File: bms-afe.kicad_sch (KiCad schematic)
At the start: 0 parts

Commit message: mostly done afe ic
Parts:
- added J2: CONN HEADER VERT 7POS 2.5MM, footprints:JST_B7B-XH-A_LF__SN_, symbol symbols:B7B-XH-A_LF__SN_
- added R39: R_Small_US, symbol Device:R_Small_US
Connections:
- new net AFEIC/U12P: J2.7, R39.1
- new net BAT_GND: J2.1
- new net CellBalance/Battery_Bottom: J2.6
- new net CellBalance1/Battery_Bottom: J2.5
- new net CellBalance2/Battery_Bottom: J2.4
- new net CellBalance3/Battery_Bottom: J2.3
- new net CellBalance4/Battery_Bottom: J2.2
- new net VBLK: R39.2
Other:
- removed sheet Balancing
- added sheet AFEIC (AFEIC.kicad_sch)
- added sheet CellBalance (CellBalance.kicad_sch)
- added sheet CellBalance1 (CellBalance.kicad_sch)
- added sheet CellBalance2 (CellBalance.kicad_sch)
- added sheet CellBalance3 (CellBalance.kicad_sch)
- added sheet CellBalance4 (CellBalance.kicad_sch)
- added sheet CellBalance5 (CellBalance.kicad_sch)

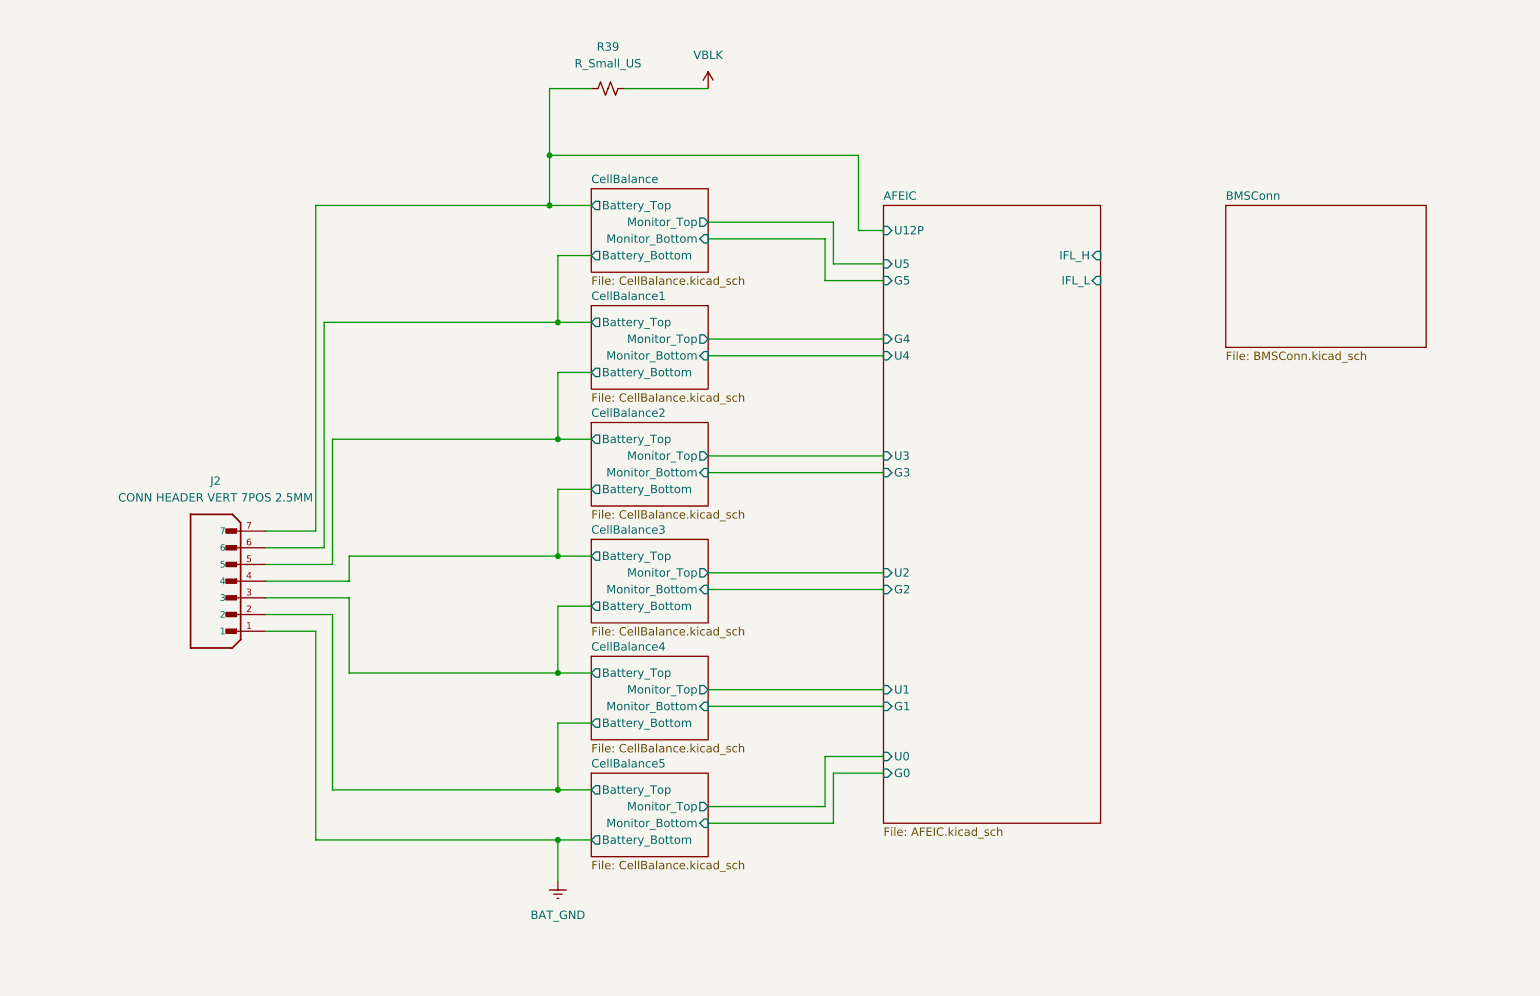
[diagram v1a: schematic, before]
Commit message: schematic done except for pulse transformer
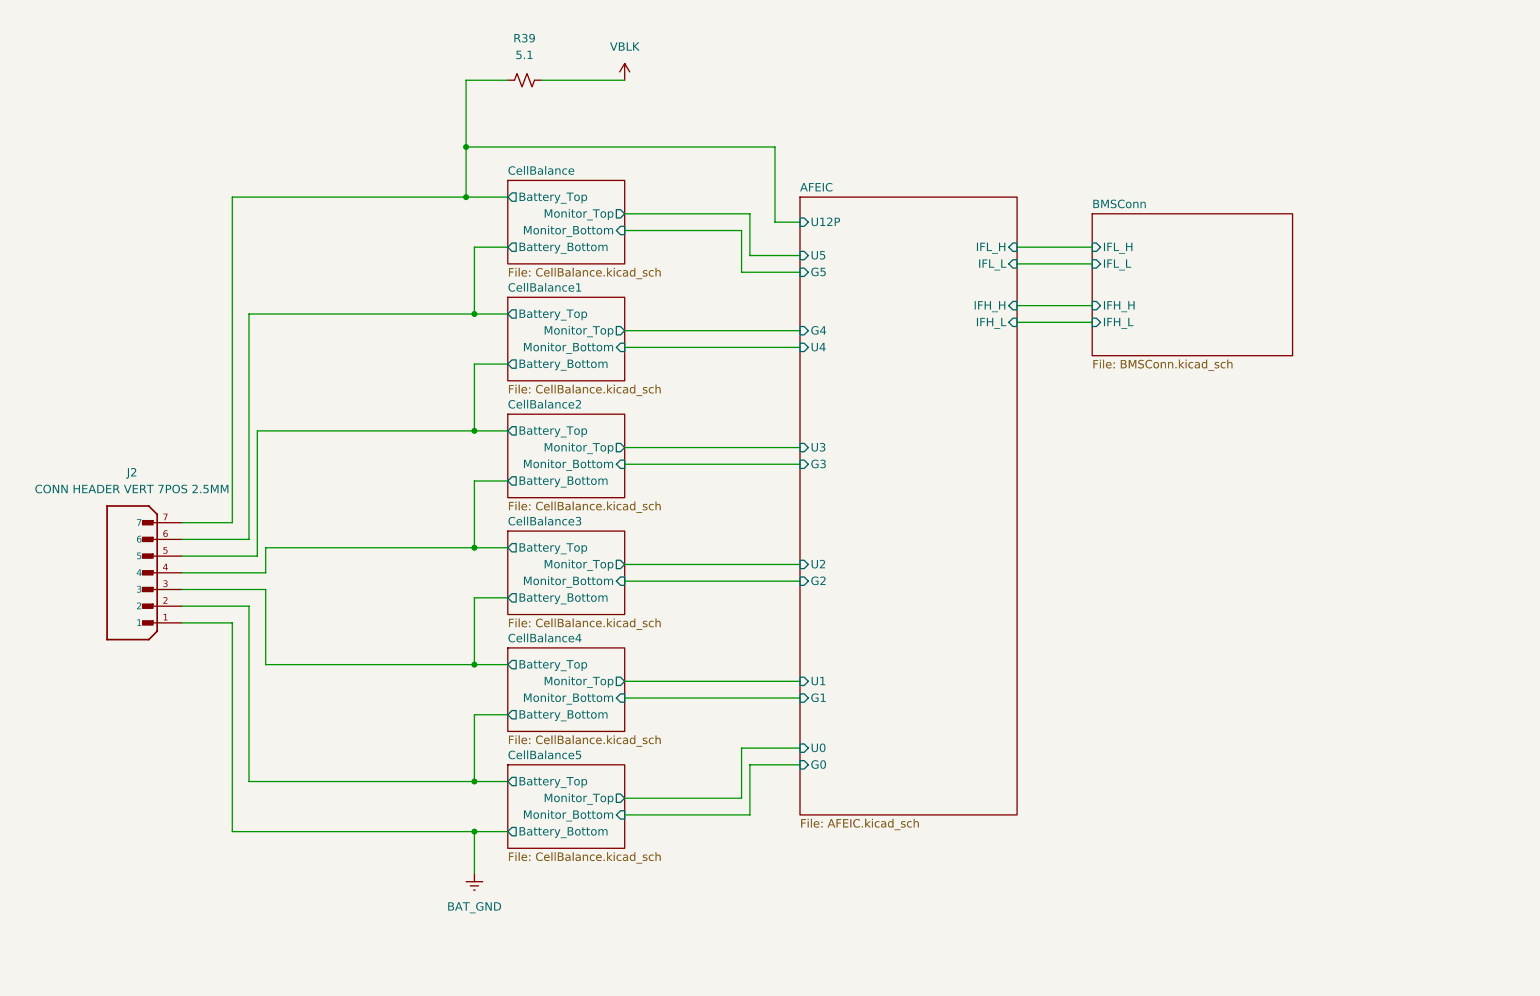
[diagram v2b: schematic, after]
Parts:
- R39: value R_Small_US -> 5.1
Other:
- sheet AFEIC ports: added IFH_H, IFH_L; removed none
- sheet BMSConn ports: added IFH_H, IFH_L, IFL_H, IFL_L; removed none
- moved on the sheet: J2, R39

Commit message: fixed balancing module and added pulse transformer
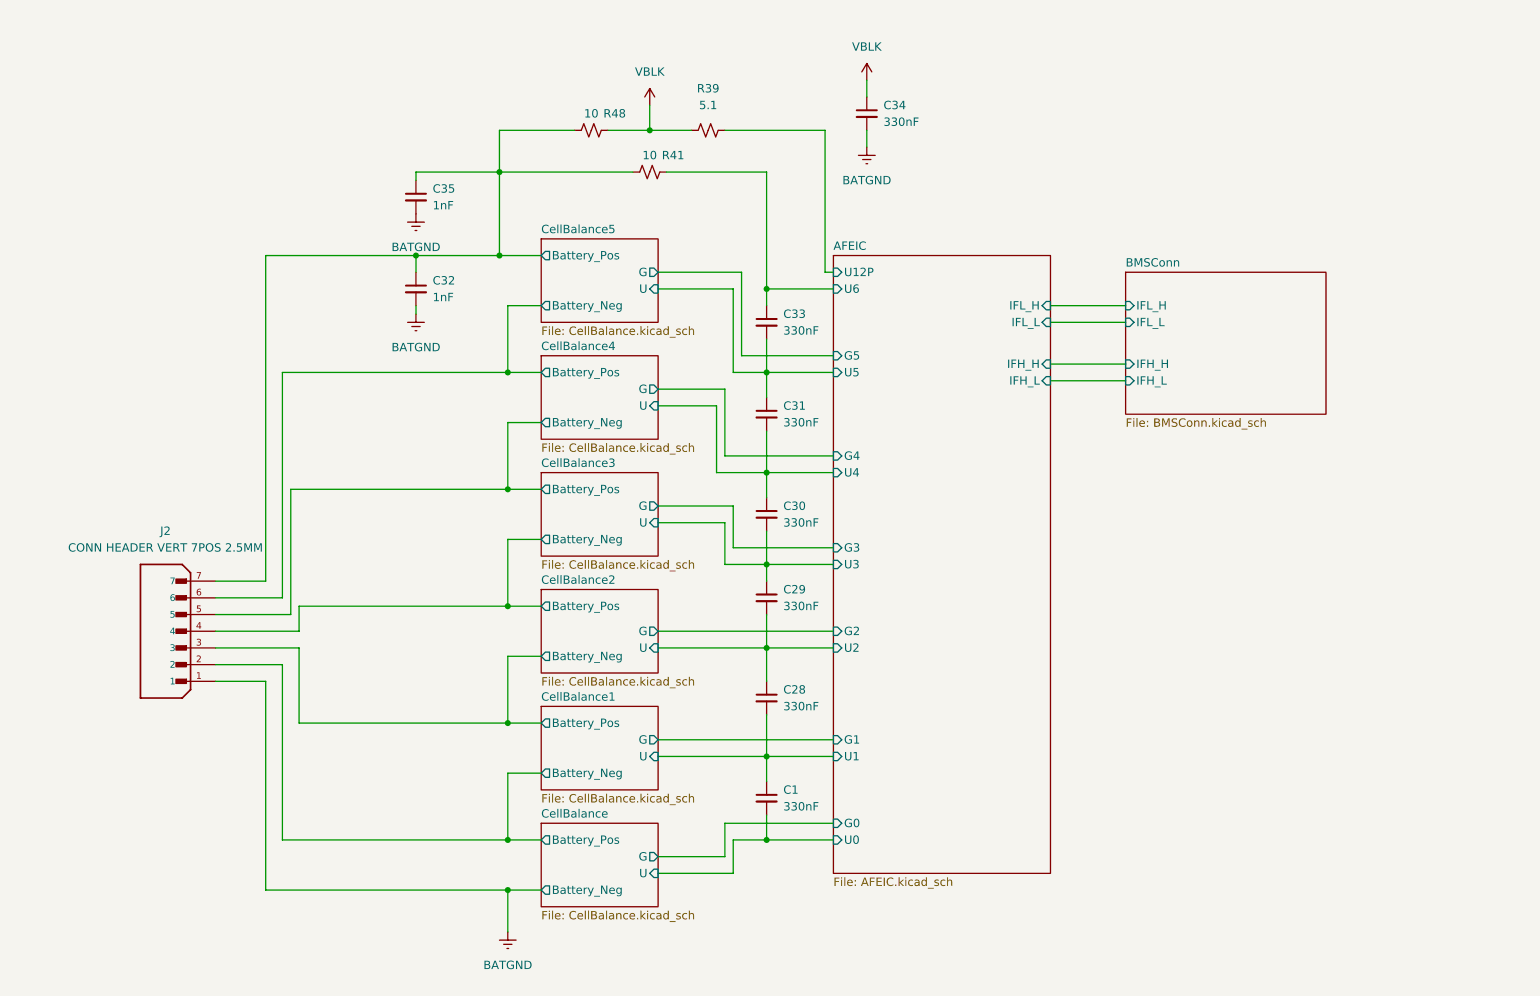
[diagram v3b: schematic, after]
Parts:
- added C1, C28, C29, C30, C31, C33, C34: 330nF, symbol Device:C_Small
- added C32, C35: 1nF, symbol Device:C_Small
- added R41, R48: 10, symbol Device:R_Small_US
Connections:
- net AFEIC/U0: now also C1.2
- net AFEIC/U1: now also C1.1, C28.2
- net AFEIC/U12P: now also R39.2; no longer J2.7, R39.1
- net AFEIC/U2: now also C28.1, C29.2
- net AFEIC/U3: now also C29.1, C30.2
- net AFEIC/U4: now also C30.1, C31.2
- net AFEIC/U5: now also C31.1, C33.2
- net VBLK: now also R39.1, C34.1, R48.2; no longer R39.2
- net BAT_GND renamed BATGND
- net BATGND: now also C32.2, C34.2, C35.2
- net CellBalance/Battery_Bottom renamed CellBalance4/Battery_Pos
- net CellBalance1/Battery_Bottom renamed CellBalance3/Battery_Pos
- net CellBalance2/Battery_Bottom renamed CellBalance2/Battery_Pos
- net CellBalance3/Battery_Bottom renamed CellBalance1/Battery_Pos
- net CellBalance4/Battery_Bottom renamed CellBalance/Battery_Pos
- new net AFEIC/U6: C33.1, R41.2
- new net CellBalance5/Battery_Pos: C32.1, C35.1, J2.7, R41.1, R48.1
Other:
- sheet AFEIC ports: added U6; removed none
- sheet CellBalance ports: added Battery_Neg, Battery_Pos, G, U; removed Battery_Bottom, Battery_Top, Monitor_Bottom, Monitor_Top
- sheet CellBalance1 ports: added Battery_Neg, Battery_Pos, G, U; removed Battery_Bottom, Battery_Top, Monitor_Bottom, Monitor_Top
- sheet CellBalance2 ports: added Battery_Neg, Battery_Pos, G, U; removed Battery_Bottom, Battery_Top, Monitor_Bottom, Monitor_Top
- sheet CellBalance3 ports: added Battery_Neg, Battery_Pos, G, U; removed Battery_Bottom, Battery_Top, Monitor_Bottom, Monitor_Top
- sheet CellBalance4 ports: added Battery_Neg, Battery_Pos, G, U; removed Battery_Bottom, Battery_Top, Monitor_Bottom, Monitor_Top
- sheet CellBalance5 ports: added Battery_Neg, Battery_Pos, G, U; removed Battery_Bottom, Battery_Top, Monitor_Bottom, Monitor_Top
- moved on the sheet: J2

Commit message: finished schematic
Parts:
- renumbered C35 to C1, C32 to C2, C33 to C3, C31 to C4, C30 to C5, C29 to C6, C28 to C7, C1 to C8, C34 to C9, J2 to J1, R48 to R1, R41 to R2, R39 to R3
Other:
- moved on the sheet: R2
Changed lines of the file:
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@@
 	(wire
 		(pts
-			(xy 115.57 41.91) (xy 135.89 41.91)
+			(xy 115.57 41.91) (xy 127 41.91)
 		)
 		(stroke
@@
 	(wire
 		(pts
-			(xy 140.97 41.91) (xy 156.21 41.91)
+			(xy 132.08 41.91) (xy 156.21 41.91)
 		)
 		(stroke
@@
 		(dnp no)
 		(fields_autoplaced yes)
-		(property "Reference" "#PWR030"
+		(property "Reference" "#PWR05"
 			(at 171.45 31.75 0)
 			(hide yes)
@@
 			(project "bms-afe"
 				(path "/226a23e7-09bb-40bc-b53a-ec42a6b7cc90"
-					(reference "#PWR030")
+					(reference "#PWR05")
 					(unit 1)
 				)
@@
 		(dnp no)
 		(fields_autoplaced yes)
-		(property "Reference" "C28"
+		(property "Reference" "C7"
 			(at 158.75 120.6562 0)
 			(show_name no)
@@
 			(project "bms-afe"
 				(path "/226a23e7-09bb-40bc-b53a-ec42a6b7cc90"
-					(reference "C28")
+					(reference "C7")
 					(unit 1)
 				)
@@
 		(dnp no)
 		(fields_autoplaced yes)
-		(property "Reference" "C1"
+		(property "Reference" "C8"
 			(at 158.75 135.8962 0)
 			(show_name no)
@@
 			(project "bms-afe"
 				(path "/226a23e7-09bb-40bc-b53a-ec42a6b7cc90"
-					(reference "C1")
+					(reference "C8")
 					(unit 1)
 				)
@@
 		(dnp no)
 		(fields_autoplaced yes)
-		(property "Reference" "#PWR027"
+		(property "Reference" "#PWR02"
 			(at 102.87 69.85 0)
 			(hide yes)
@@
 			(project "bms-afe"
 				(path "/226a23e7-09bb-40bc-b53a-ec42a6b7cc90"
-					(reference "#PWR027")
+					(reference "#PWR02")
 					(unit 1)
 				)
@@
 		(dnp no)
 		(fields_autoplaced yes)
-		(property "Reference" "C35"
+		(property "Reference" "C1"
 			(at 105.41 44.4562 0)
 			(show_name no)
@@
 			(project "bms-afe"
 				(path "/226a23e7-09bb-40bc-b53a-ec42a6b7cc90"
-					(reference "C35")
+					(reference "C1")
 					(unit 1)
 				)
@@
 	(symbol
 		(lib_id "Device:R_Small_US")
-		(at 138.43 41.91 90)
-		(unit 1)
-		(body_style 1)
-		(exclude_from_sim no)
-		(in_bom yes)
-		(on_board yes)
-		(in_pos_files yes)
-		(dnp no)
-		(property "Reference" "R41"
-			(at 141.986 39.37 90)
+		(at 129.54 41.91 90)
+		(unit 1)
+		(body_style 1)
+		(exclude_from_sim no)
+		(in_bom yes)
+		(on_board yes)
+		(in_pos_files yes)
+		(dnp no)
+		(property "Reference" "R2"
+			(at 133.096 39.37 90)
 			(show_name no)
 			(do_not_autoplace no)
@@
 		)
 		(property "Value" "10"
-			(at 138.43 39.37 90)
+			(at 129.54 39.37 90)
 			(show_name no)
 			(do_not_autoplace no)
@@
 		)
 		(property "Footprint" ""
-			(at 138.43 41.91 0)
+			(at 129.54 41.91 0)
 			(hide yes)
 			(show_name no)
@@
 		)
 		(property "Datasheet" ""
-			(at 138.43 41.91 0)
+			(at 129.54 41.91 0)
 			(hide yes)
 			(show_name no)
@@
 		)
 		(property "Description" "Resistor, small US symbol"
-			(at 138.43 41.91 0)
+			(at 129.54 41.91 0)
 			(hide yes)
 			(show_name no)
@@
 			(project "bms-afe"
 				(path "/226a23e7-09bb-40bc-b53a-ec42a6b7cc90"
-					(reference "R41")
+					(reference "R2")
 					(unit 1)
 				)
@@
 		(dnp no)
 		(fields_autoplaced yes)
-		(property "Reference" "C33"
+		(property "Reference" "C3"
 			(at 158.75 63.5062 0)
 			(show_name no)
@@
 			(project "bms-afe"
 				(path "/226a23e7-09bb-40bc-b53a-ec42a6b7cc90"
-					(reference "C33")
+					(reference "C3")
 					(unit 1)
 				)
@@
 		(dnp no)
 		(fields_autoplaced yes)
-		(property "Reference" "J2"
+		(property "Reference" "J1"
 			(at 64.77 96.52 0)
 			(show_name no)
@@
 			(project "bms-afe"
 				(path "/226a23e7-09bb-40bc-b53a-ec42a6b7cc90"
-					(reference "J2")
+					(reference "J1")
 					(unit 1)
 				)
@@
 		(dnp no)
 		(fields_autoplaced yes)
-		(property "Reference" "#PWR02"
+		(property "Reference" "#PWR04"
 			(at 138.43 35.56 0)
 			(hide yes)
@@
 			(project "bms-afe"
 				(path "/226a23e7-09bb-40bc-b53a-ec42a6b7cc90"
-					(reference "#PWR02")
+					(reference "#PWR04")
 					(unit 1)
 				)
@@
 		(dnp no)
 		(fields_autoplaced yes)
-		(property "Reference" "R39"
+		(property "Reference" "R3"
 			(at 147.32 29.21 90)
 			(show_name no)
@@
 			(project "bms-afe"
 				(path "/226a23e7-09bb-40bc-b53a-ec42a6b7cc90"
-					(reference "R39")
+					(reference "R3")
 					(unit 1)
 				)
@@
 		(in_pos_files yes)
 		(dnp no)
-		(property "Reference" "R48"
+		(property "Reference" "R1"
 			(at 133.096 33.02 90)
 			(show_name no)
@@
 			(project "bms-afe"
 				(path "/226a23e7-09bb-40bc-b53a-ec42a6b7cc90"
-					(reference "R48")
+					(reference "R1")
 					(unit 1)
 				)
@@
 		(dnp no)
 		(fields_autoplaced yes)
-		(property "Reference" "C34"
+		(property "Reference" "C9"
 			(at 173.99 31.7562 0)
 			(show_name no)
@@
 			(project "bms-afe"
 				(path "/226a23e7-09bb-40bc-b53a-ec42a6b7cc90"
-					(reference "C34")
+					(reference "C9")
 					(unit 1)
 				)
@@
 		(dnp no)
 		(fields_autoplaced yes)
-		(property "Reference" "C30"
+		(property "Reference" "C5"
 			(at 158.75 92.7162 0)
 			(show_name no)
@@
 			(project "bms-afe"
 				(path "/226a23e7-09bb-40bc-b53a-ec42a6b7cc90"
-					(reference "C30")
+					(reference "C5")
 					(unit 1)
 				)
@@
 		(dnp no)
 		(fields_autoplaced yes)
-		(property "Reference" "#PWR012"
+		(property "Reference" "#PWR03"
 			(at 116.84 163.83 0)
 			(hide yes)
@@
 			(project "bms-afe"
 				(path "/226a23e7-09bb-40bc-b53a-ec42a6b7cc90"
-					(reference "#PWR012")
+					(reference "#PWR03")
 					(unit 1)
 				)
@@
 		(dnp no)
 		(fields_autoplaced yes)
-		(property "Reference" "C32"
+		(property "Reference" "C2"
 			(at 105.41 58.4262 0)
 			(show_name no)
@@
 			(project "bms-afe"
 				(path "/226a23e7-09bb-40bc-b53a-ec42a6b7cc90"
-					(reference "C32")
+					(reference "C2")
 					(unit 1)
 				)
@@
 		(dnp no)
 		(fields_autoplaced yes)
-		(property "Reference" "#PWR028"
+		(property "Reference" "#PWR06"
 			(at 171.45 44.45 0)
 			(hide yes)
@@
 			(project "bms-afe"
 				(path "/226a23e7-09bb-40bc-b53a-ec42a6b7cc90"
-					(reference "#PWR028")
+					(reference "#PWR06")
 					(unit 1)
 				)
@@
 		(dnp no)
 		(fields_autoplaced yes)
-		(property "Reference" "C29"
+		(property "Reference" "C6"
 			(at 158.75 105.4162 0)
 			(show_name no)
@@
 			(project "bms-afe"
 				(path "/226a23e7-09bb-40bc-b53a-ec42a6b7cc90"
-					(reference "C29")
+					(reference "C6")
 					(unit 1)
 				)
@@
 		(dnp no)
 		(fields_autoplaced yes)
-		(property "Reference" "C31"
+		(property "Reference" "C4"
 			(at 158.75 77.4762 0)
 			(show_name no)
@@
 			(project "bms-afe"
 				(path "/226a23e7-09bb-40bc-b53a-ec42a6b7cc90"
-					(reference "C31")
+					(reference "C4")
 					(unit 1)
 				)
@@
 		(dnp no)
 		(fields_autoplaced yes)
-		(property "Reference" "#PWR029"
+		(property "Reference" "#PWR01"
 			(at 102.87 54.61 0)
 			(hide yes)
@@
 			(project "bms-afe"
 				(path "/226a23e7-09bb-40bc-b53a-ec42a6b7cc90"
-					(reference "#PWR029")
-					(unit 1)
-				)
+					(reference "#PWR01")
+					(unit 1)
+				)

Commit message: fixed minor changes
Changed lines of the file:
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@@
 		(in_pos_files yes)
 		(dnp no)
-		(fields_autoplaced yes)
 		(property "Reference" "#PWR01"
 			(at 102.87 54.61 0)
@@
 		)
 		(property "Value" "BATGND"
-			(at 102.87 53.34 0)
+			(at 96.266 49.784 0)
 			(show_name no)
 			(do_not_autoplace no)

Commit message: passive values
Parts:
- removed C1, C2: 1nF, symbol Device:C_Small
- removed C3, C4, C5, C6, C7, C8, C9: 330nF, symbol Device:C_Small
- added C11, C13: CAP CER 0603 1NF 16V X7R 10%, Capacitor_SMD:C_0603_1608Metric, symbol Device:C_Small
- added C54, C55, C56, C57, C58, C59, C60: CAP CER 0.33UF 16V X7R 0603, Capacitor_SMD:C_0603_1608Metric, symbol Device:C_Small
- R1, R2: value 10 -> RES 10 OHM 1% 1/10W 0603; footprint (none) -> Resistor_SMD:R_0603_1608Metric
- R3: value 5.1 -> RES SMD 5.1 OHM 1% 1/8W 0603; footprint (none) -> Resistor_SMD:R_0603_1608Metric; LCSC (none) -> C242492
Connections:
- net AFEIC/U0: now also C59.2
- net AFEIC/U1: now also C58.2, C59.1
- net AFEIC/U2: now also C57.2, C58.1
- net AFEIC/U3: now also C56.2, C57.1
- net AFEIC/U4: now also C55.2, C56.1
- net AFEIC/U5: now also C54.2, C55.1
- net AFEIC/U6: now also C54.1
- net BATGND: now also C11.1, C13.1, C60.2
- net CellBalance5/Battery_Pos: now also C11.2, C13.2
- net VBLK: now also C60.1
